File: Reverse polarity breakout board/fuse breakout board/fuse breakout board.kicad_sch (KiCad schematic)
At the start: 7 parts

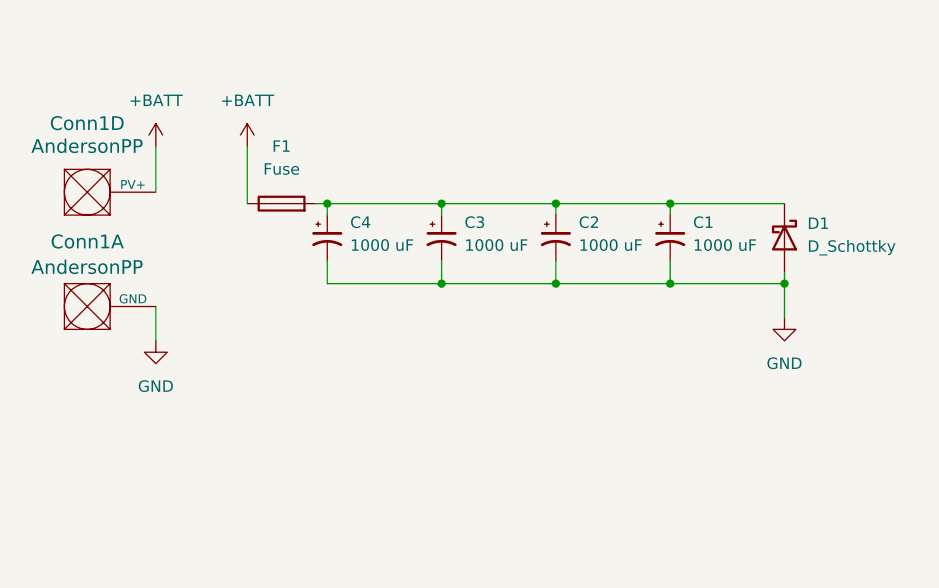
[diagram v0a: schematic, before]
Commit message: Added Load Tester andersons and via stitching
Added load tester andersons and vias to stitch ground planes on the front and back together to prevent capacitance build up and allow current to flow
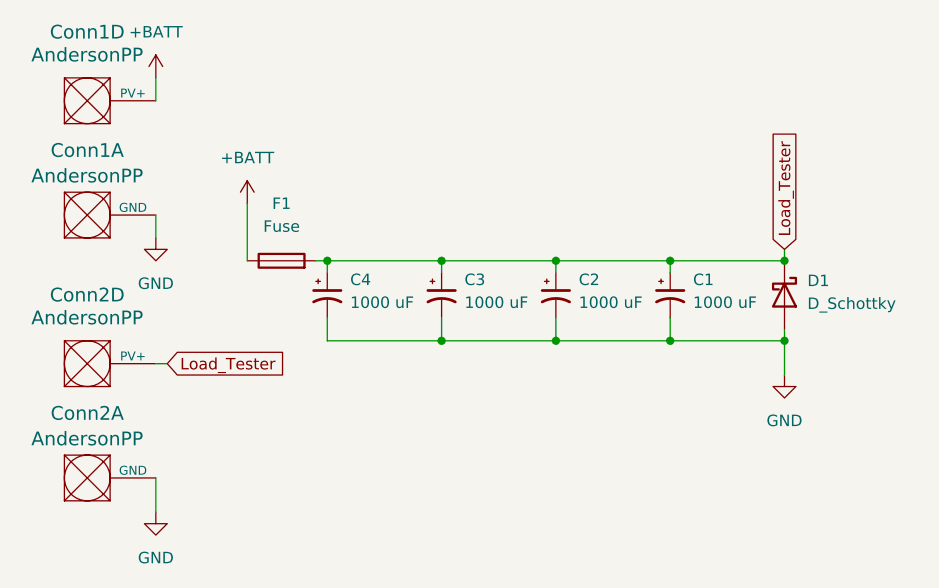
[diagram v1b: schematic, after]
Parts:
- added Conn2: AndersonPP, MRDT_Connectors:Square_Anderson_2_H_Side_By_Side_PV, symbol MRDT_Connectors:AndersonPP
- Conn1: footprint MRDT_Connectors:Square_Anderson_1_H -> MRDT_Connectors:Square_Anderson_2_H_Side_By_Side_PV
- Conn1: footprint (none) -> MRDT_Connectors:Square_Anderson_2_H_Side_By_Side_PV
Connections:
- net GND: now also Conn2.1 (GND)
- net Load_Tester: now reaches C1.1, C2.1, C3.1, C4.1, D1.1 (K), F1.2
- net Load_Tester: now also Conn2.4 (PV+)
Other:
- moved on the sheet: C1, C2, C3, C4, Conn1A, Conn1D, D1, F1
